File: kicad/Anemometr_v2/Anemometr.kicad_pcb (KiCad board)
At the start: 2 copper layers, 45 x 45 mm, 156 parts, among them J1 TxD, J10 +Z1, J11 +Z2, J12 +Z3, J13 +Z4, J14 -Z1, J15 -Z2, J16 -Z3, J17 -Z4, J18 1 TxD+, J19 2 TxD-, J2 RxD, J20 3 RxD+, J21 4-5, J22 6 RxD-, J23 7-8, J24 Conn_01x01_Female, J3 SCL, J4 SDA, J5 RST, J6 +EXT, J7 -EXT, J8 SWD, J9 SWC, Q1 5N10, U1 STM32F103C8Tx, U2 TS5A3166DBVR, U3 TS5A3166DBVR, U4 TS5A3166DBVR, U5 TS5A3166DBVR, U6 NCP1117-3.3, U7 MCP1703-5, U8 TLV3201DBV, U9 MCP1703-3.3, Y1 CSTCE8M00G52A-R0, Y2 QC5CB25.0000F18B23R

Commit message: изменено:      kicad/Anemometr_v2/Anemometr.kicad_pcb 	изменено:      kicad/Anemometr_v2/Anemometr.kicad_pcb-bak 	изменено:      stm32cubeide/Anemometer/.settings/language.settings.xml 	изменено:      stm32cubeide/Anemometer/Core/Inc/main.h 	изменено:      stm32cubeide/Anemometer/Core/Src/main.c 	изменено:      stm32cubeide/Anemometer/Core/Src/stm32f1xx_it.c 	изменено:      stm32cubeide/Anemometer/Release/Core/Src/main.su 	изменено:      stm32cubeide/Anemometer/Release/makefile
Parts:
- moved D5 4.56 mm to (59.9, 67.5)
- moved R15 1.47 mm to (59.9, 64.6), turned to 90 degrees
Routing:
- net Net-(D10-Pad10): track 18.5 -> 18.0 mm
- net GND: vias 22 -> 25

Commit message: изменено:      kicad/Anemometr_v2/Anemometr-cache.lib 	изменено:      kicad/Anemometr_v2/Anemometr.kicad_pcb 	изменено:      kicad/Anemometr_v2/Anemometr.kicad_pcb-bak 	изменено:      kicad/Anemometr_v2/Anemometr.sch 	изменено:      kicad/Anemometr_v2/Anemometr.sch-bak 	изменено:      kicad/Anemometr_v2/fp-info-cache 	изменено:      kicad/Anemometr_v2/gerber/Anemometr-job.gbrjob 	изменено:      kicad/Anemometr_v2/gerber/Border.gbr 	изменено:      kicad/Anemometr_v2/gerber/Bottom.gbr 	изменено:      kicad/Anemometr_v2/gerber/MaskBottom.gbr 	изменено:      kicad/Anemometr_v2/gerber/MaskTop.gbr 	изменено:      kicad/Anemometr_v2/gerber/NCData.drl 	изменено:      kicad/Anemometr_v2/gerber/Top.gbr 	изменено:      kicad/Anemometr_v2/gerber/anemometr.zip
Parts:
- added J25: Conn_01x01_Female, My-library:SMD-CONN, B.Cu at (39.4, 66.0)
- Y2: value QC5CB25.0000F18B23R -> ECS-250-20-33; footprint Crystal:Crystal_SMD_Qantek_QC5CB-2Pin_5x3.2mm -> Crystal:Crystal_SMD_SeikoEpson_FA238-4Pin_3.2x2.5mm
- moved R1 4.43 mm to (55.7, 86.3)
- moved C23 3.83 mm to (24.2, 63.4), turned to 0 degrees
- moved C4 3.65 mm to (53.1, 84.2)
- moved C7 2.22 mm to (58.4, 84.2), turned to 270 degrees
- moved U7 1.59 mm to (23.9, 67.2)
- moved J24 1.40 mm to (34.0, 69.2)
- moved R31 1.32 mm to (28.4, 66.7), turned to 180 degrees
- moved C37 1.21 mm to (28.8, 62.9)
- moved J6 0.89 mm to (31.0, 64.0)
- moved D8 0.43 mm to (30.6, 85.8)
- moved C29 0.43 mm to (24.7, 88.4)
- moved R19 0.43 mm to (31.4, 88.4)
- moved R28 0.43 mm to (23.4, 88.4)
- moved C33 0.43 mm to (26.9, 86.2)
- moved R21 0.43 mm to (27.4, 88.4)
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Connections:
- Y2 pad 2: Net-(C7-Pad1) -> GND
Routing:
- net GND: track 150.8 -> 165.9 mm, vias 25 -> 26
- net Net-(C4-Pad1): track 9.88 -> 6.20 mm
- net +5VA: track 51.7 -> 48.6 mm
- net /5.6-6v: track 70.8 -> 68.5 mm
- net Net-(C47-Pad2): track 3.23 -> 5.06 mm
- net Net-(D14-Pad2): track 18.2 -> 17.0 mm
- net SensorInput: track 6.92 -> 6.30 mm
- net +3V3: track 45.1 -> 44.6 mm

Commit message: изменено:      kicad/Anemometr_v2/Anemometr.kicad_pcb 	изменено:      kicad/Anemometr_v2/Anemometr.kicad_pcb-bak 	изменено:      kicad/Anemometr_v2/gerber/Anemometr-job.gbrjob 	изменено:      kicad/Anemometr_v2/gerber/Border.gbr 	изменено:      kicad/Anemometr_v2/gerber/Bottom.gbr 	изменено:      kicad/Anemometr_v2/gerber/MaskBottom.gbr 	изменено:      kicad/Anemometr_v2/gerber/MaskTop.gbr 	изменено:      kicad/Anemometr_v2/gerber/NCData.drl 	изменено:      kicad/Anemometr_v2/gerber/Top.gbr 	изменено:      kicad/Anemometr_v2/gerber/anemometr.zip
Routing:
- net Net-(C19-Pad1): track 48.9 -> 47.9 mm

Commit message: изменено:      kicad/Anemometr_v2/Anemometr-cache.lib 	изменено:      kicad/Anemometr_v2/Anemometr.kicad_pcb 	изменено:      kicad/Anemometr_v2/Anemometr.kicad_pcb-bak 	изменено:      kicad/Anemometr_v2/Anemometr.sch 	изменено:      kicad/Anemometr_v2/Anemometr.sch-bak
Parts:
- D1: value LED -> Act
- D2: value LED -> Link
- moved C51 7.47 mm to (41.8, 72.0)
- moved C47 3.87 mm to (34.4, 69.1)
- moved J25 3.66 mm to (37.0, 68.8)
- moved J24 3.56 mm to (33.0, 72.5)
- moved R38 3.31 mm to (39.5, 72.0)
- moved R37 2.93 mm to (39.6, 67.5), turned to 0 degrees
- moved R39 2.60 mm to (38.9, 69.8)
- moved C59 2.60 mm to (40.3, 69.8)
- moved U8 1.34 mm to (36.3, 71.6), turned to 0 degrees
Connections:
- C47 pad 2: Net-(C47-Pad2) -> Analog
- J25 pad 1: Net-(C47-Pad2) -> Analog
- R37 pad 1: Net-(C47-Pad2) -> Analog
- U1 pad 18: (no net) -> Analog
- U8 pad 3: Net-(C47-Pad2) -> Analog
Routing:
- net GND: track 165.9 -> 178.7 mm
- net Analog: track 0.00 -> 10.8 mm, vias 0 -> 1
- net Net-(C47-Pad2): track 5.06 -> 0.00 mm
- net +3V3: track 44.6 -> 46.7 mm
- net SensorInput: track 6.27 -> 5.51 mm

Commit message: изменено:      Release/all.zip 	изменено:      Release/mk.sh 	изменено:      kicad/Anemometr_v2/Anemometr.kicad_pcb 	изменено:      kicad/Anemometr_v2/Anemometr.kicad_pcb-bak 	изменено:      kicad/Anemometr_v2/bom/ibom.html 	изменено:      kicad/Anemometr_v2/gerber/Anemometr-job.gbrjob 	изменено:      kicad/Anemometr_v2/gerber/Border.gbr 	изменено:      kicad/Anemometr_v2/gerber/Bottom.gbr 	изменено:      kicad/Anemometr_v2/gerber/MaskBottom.gbr 	изменено:      kicad/Anemometr_v2/gerber/MaskTop.gbr 	изменено:      kicad/Anemometr_v2/gerber/NCData.drl 	изменено:      kicad/Anemometr_v2/gerber/Top.gbr 	изменено:      kicad/Anemometr_v2/gerber/anemometr.zip
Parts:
- C57: value 15p -> 51p

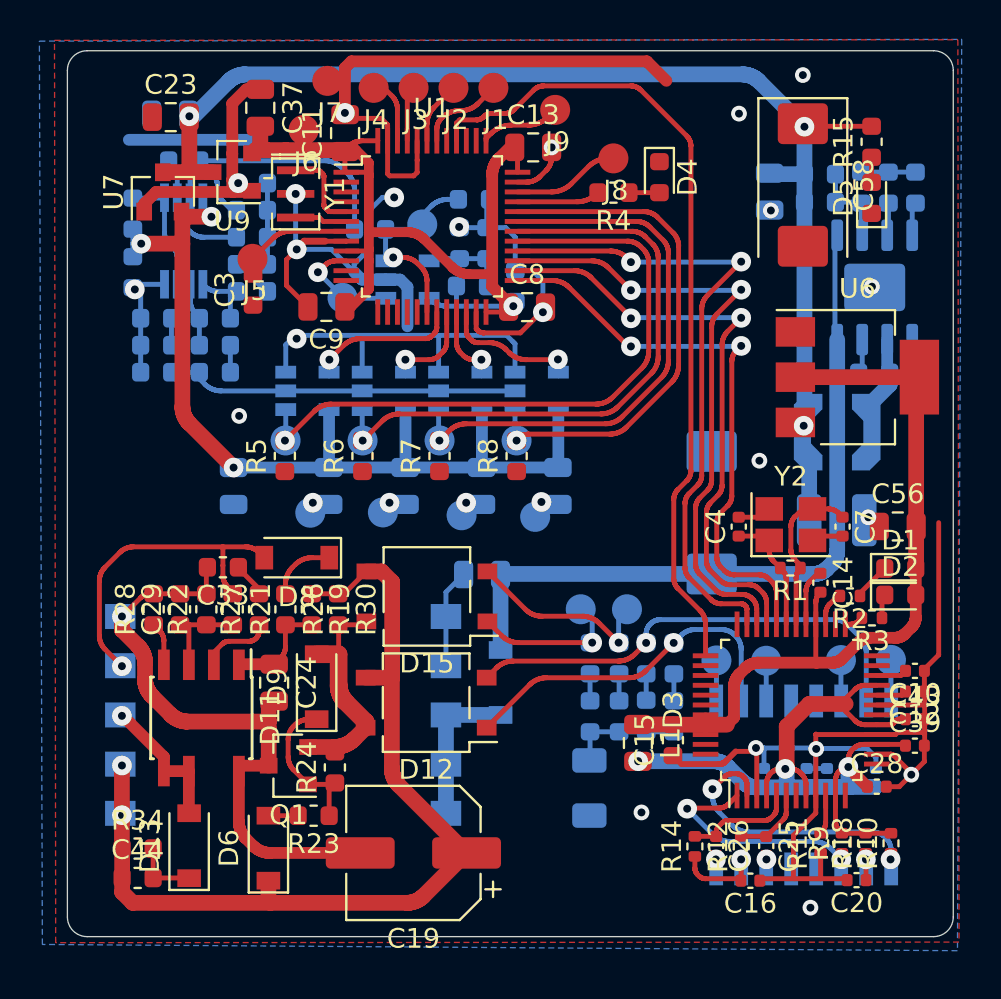
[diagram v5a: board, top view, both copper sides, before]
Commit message: изменено:      FreeCAD/holder-3.fcstd 	изменено:      kicad/Anemometr_v2/Anemometr.kicad_pcb 	изменено:      kicad/Anemometr_v2/Anemometr.kicad_pcb-bak 	изменено:      kicad/Anemometr_v2/Anemometr.sch 	изменено:      kicad/Anemometr_v2/Anemometr.sch-bak 	изменено:      kicad/Anemometr_v2/fp-info-cache
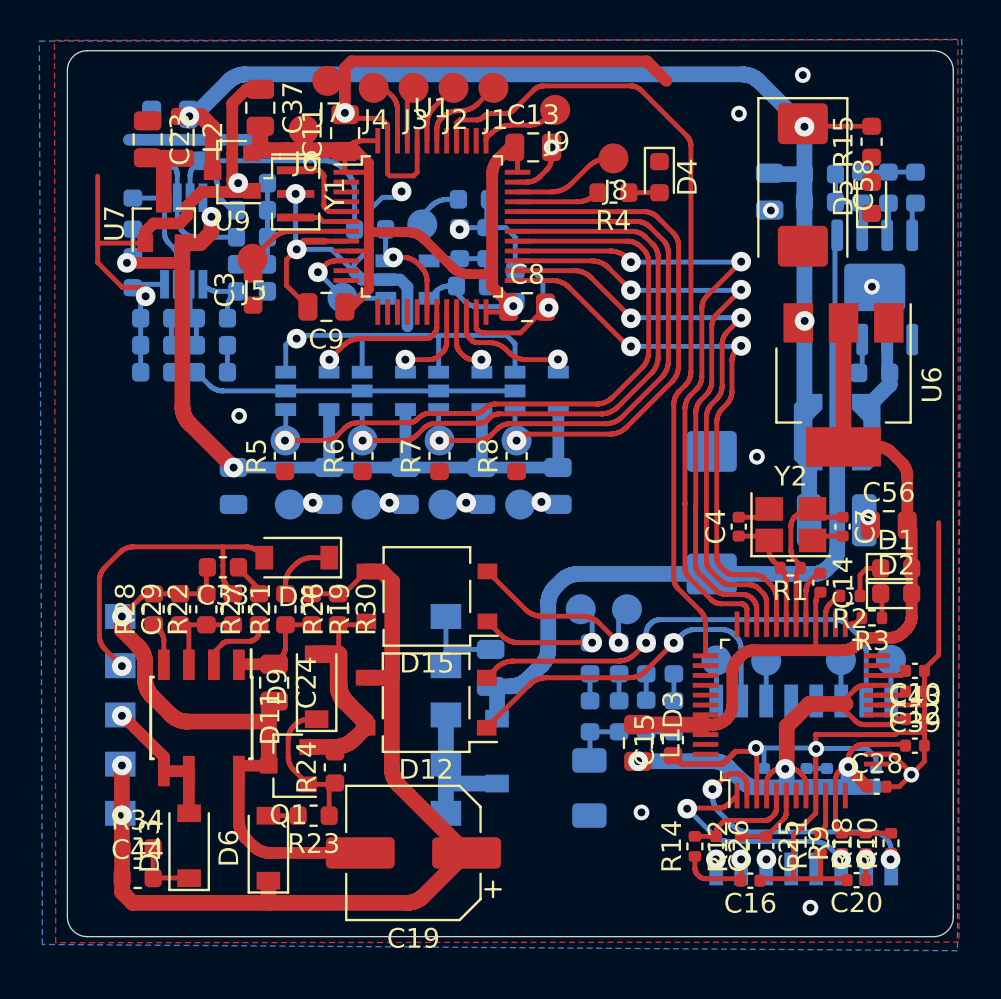
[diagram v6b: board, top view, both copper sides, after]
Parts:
- added L2: 47uH, Inductor_SMD:L_0805_2012Metric, F.Cu at (24.9, 64.4)
- moved C30 4.76 mm to (40.5, 91.3), turned to 270 degrees
- moved D16 3.49 mm to (40.8, 95.6)
- moved C23 1.63 mm to (23.1, 64.5), turned to 270 degrees
- moved U7 1.60 mm to (23.9, 68.8)
- moved J15 1.12 mm to (30.3, 83.0)
- moved J17 1.07 mm to (38.1, 83.0)
- moved J16 0.99 mm to (42.0, 83.0)
- moved J14 0.92 mm to (34.2, 83.0)
- moved U6 0.81 mm to (58.4, 77.0), turned to 270 degrees
- moved C56 0.46 mm to (60.7, 84.1)
- moved D2 0.22 mm to (61.1, 87.6)
- moved D1 0.21 mm to (61.1, 86.3)
- moved C18 0.15 mm to (26.3, 76.3)
- moved R20 0.15 mm to (26.3, 75.0)
- moved R25 0.15 mm to (26.3, 73.6)
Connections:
- C23 pad 2: /5.6-6v -> Net-(C23-Pad2)
- U7 pad 3: /5.6-6v -> Net-(C23-Pad2)
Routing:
- net GND: track 178.7 -> 189.2 mm
- net Net-(C23-Pad2): track 0.00 -> 4.15 mm
- net /12-16v: track 37.8 -> 40.2 mm
- net /5.6-6v: track 68.5 -> 66.8 mm
- net +3.3VDAC: track 40.6 -> 39.3 mm
